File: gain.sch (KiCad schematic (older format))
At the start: 9 parts, among them U11 NE5532

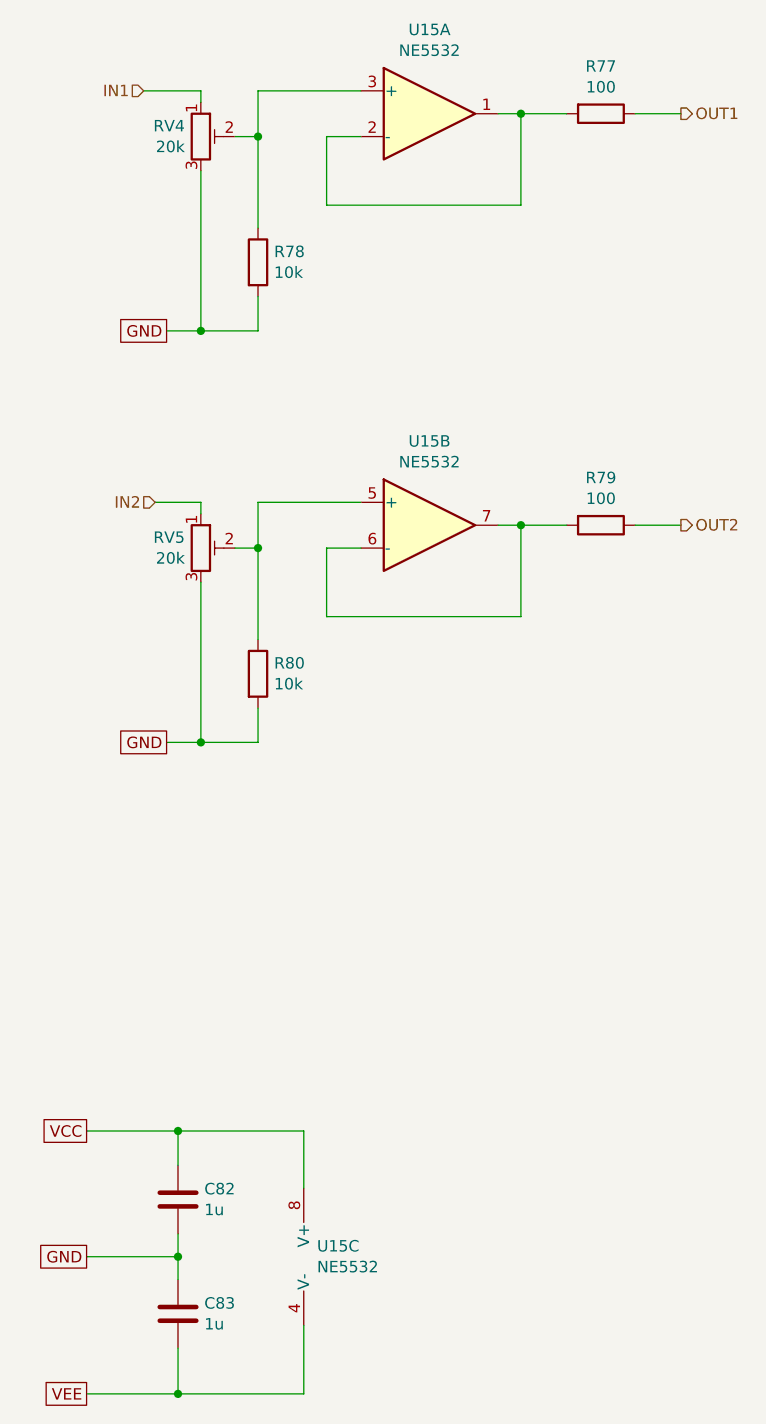
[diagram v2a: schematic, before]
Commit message: inverted LF processing chain, now with BW2 subsonic filter
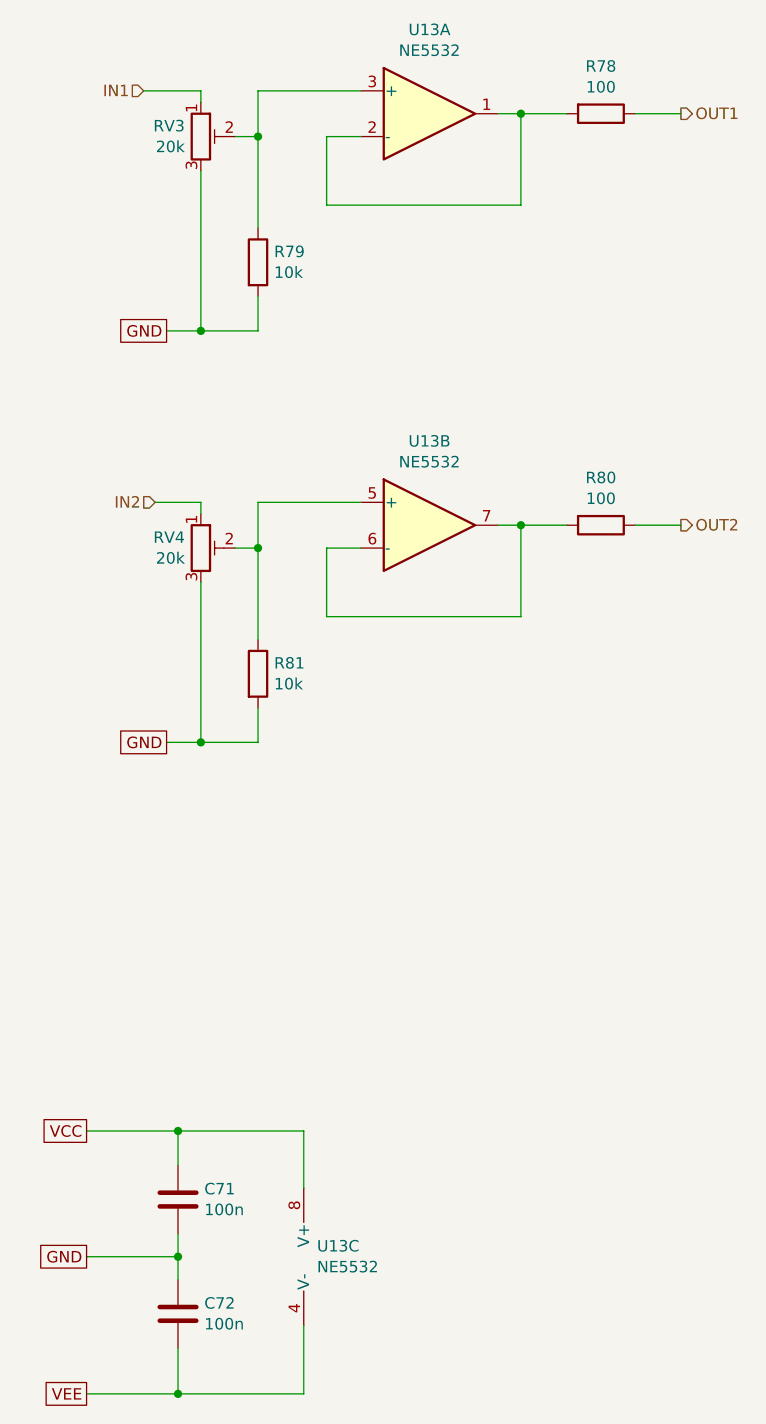
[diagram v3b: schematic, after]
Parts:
- C59: renamed from C58; value 1u -> 100n
- C60: renamed from C59; value 1u -> 100n
- renumbered RV2 to RV1, RV3 to RV2
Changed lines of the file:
@@
 $Descr A4 11693 8268
 encoding utf-8
-Sheet 13 19
+Sheet 10 17
 Title "Output Gain Controls"
 Date "2021-10-03"
@@
 AR Path="/615C4B54/61606DFA" Ref="U?"  Part="3"
 AR Path="/61604458/61606DFA" Ref="U11"  Part="3"
-AR Path="/6164D7C0/61606DFA" Ref="U15"  Part="3"
+AR Path="/6164D7C0/61606DFA" Ref="U13"  Part="3"
 AR Path="/61651AA2/61606DFA" Ref="U?"  Part="3"
-F 0 "U15" H 2808 6846 50  0000 L CNN
+F 0 "U13" H 2808 6846 50  0000 L CNN
 F 1 "NE5532" H 2808 6755 50  0000 L CNN
 F 2 "Housings_DIP:DIP-8_W7.62mm_Socket" H 2850 6800 50  0001 C CNN
@@
 AR Path="/61597701/61606E00" Ref="C?"  Part="1"
 AR Path="/615C4B54/61606E00" Ref="C?"  Part="1"
-AR Path="/61604458/61606E00" Ref="C59"  Part="1"
-AR Path="/6164D7C0/61606E00" Ref="C83"  Part="1"
+AR Path="/61604458/61606E00" Ref="C60"  Part="1"
+AR Path="/6164D7C0/61606E00" Ref="C72"  Part="1"
 AR Path="/61651AA2/61606E00" Ref="C?"  Part="1"
-F 0 "C83" H 2315 7096 50  0000 L CNN
-F 1 "1u" H 2315 7005 50  0000 L CNN
+F 0 "C72" H 2315 7096 50  0000 L CNN
+F 1 "100n" H 2315 7005 50  0000 L CNN
 F 2 "Capacitors_SMD:C_0805" H 2238 6900 50  0001 C CNN
 F 3 "~" H 2200 7050 50  0001 C CNN
@@
 AR Path="/61597701/61606E06" Ref="C?"  Part="1"
 AR Path="/615C4B54/61606E06" Ref="C?"  Part="1"
-AR Path="/61604458/61606E06" Ref="C58"  Part="1"
-AR Path="/6164D7C0/61606E06" Ref="C82"  Part="1"
+AR Path="/61604458/61606E06" Ref="C59"  Part="1"
+AR Path="/6164D7C0/61606E06" Ref="C71"  Part="1"
 AR Path="/61651AA2/61606E06" Ref="C?"  Part="1"
-F 0 "C82" H 2315 6596 50  0000 L CNN
-F 1 "1u" H 2315 6505 50  0000 L CNN
+F 0 "C71" H 2315 6596 50  0000 L CNN
+F 1 "100n" H 2315 6505 50  0000 L CNN
 F 2 "Capacitors_SMD:C_0805" H 2238 6400 50  0001 C CNN
 F 3 "~" H 2200 6550 50  0001 C CNN
@@
 P 3300 1800
 AR Path="/61604458/6160713F" Ref="U11"  Part="1"
-AR Path="/6164D7C0/6160713F" Ref="U15"  Part="1"
+AR Path="/6164D7C0/6160713F" Ref="U13"  Part="1"
 AR Path="/61651AA2/6160713F" Ref="U?"  Part="1"
-F 0 "U15" H 3300 2167 50  0000 C CNN
+F 0 "U13" H 3300 2167 50  0000 C CNN
 F 1 "NE5532" H 3300 2076 50  0000 C CNN
 F 2 "" H 3300 1800 50  0001 C CNN
@@
 P 3300 3600
 AR Path="/61604458/61607B4F" Ref="U11"  Part="2"
-AR Path="/6164D7C0/61607B4F" Ref="U15"  Part="2"
+AR Path="/6164D7C0/61607B4F" Ref="U13"  Part="2"
 AR Path="/61651AA2/61607B4F" Ref="U?"  Part="2"
-F 0 "U15" H 3300 3967 50  0000 C CNN
+F 0 "U13" H 3300 3967 50  0000 C CNN
 F 1 "NE5532" H 3300 3876 50  0000 C CNN
 F 2 "" H 3300 3600 50  0001 C CNN
@@
 $EndComp
 $Comp
-L Device:R_POT_TRIM RV2
+L Device:R_POT_TRIM RV1
 U 1 1 6160B080
 P 2300 1900
-AR Path="/61604458/6160B080" Ref="RV2"  Part="1"
-AR Path="/6164D7C0/6160B080" Ref="RV4"  Part="1"
+AR Path="/61604458/6160B080" Ref="RV1"  Part="1"
+AR Path="/6164D7C0/6160B080" Ref="RV3"  Part="1"
 AR Path="/61651AA2/6160B080" Ref="RV?"  Part="1"
-F 0 "RV4" H 2230 1946 50  0000 R CNN
+F 0 "RV3" H 2230 1946 50  0000 R CNN
 F 1 "20k" H 2230 1855 50  0000 R CNN
 F 2 "Potentiometers:Potentiometer_Trimmer_Bourns_3296W" H 2300 1900 50  0001 C CNN
@@
 P 2550 2450
 AR Path="/61604458/6160B89B" Ref="R54"  Part="1"
-AR Path="/6164D7C0/6160B89B" Ref="R78"  Part="1"
+AR Path="/6164D7C0/6160B89B" Ref="R79"  Part="1"
 AR Path="/61651AA2/6160B89B" Ref="R?"  Part="1"
-F 0 "R78" H 2620 2496 50  0000 L CNN
+F 0 "R79" H 2620 2496 50  0000 L CNN
 F 1 "10k" H 2620 2405 50  0000 L CNN
 F 2 "Resistors_SMD:R_0805" V 2480 2450 50  0001 C CNN
@@
 	2300 1700 2300 1750
 $Comp
-L Device:R_POT_TRIM RV3
+L Device:R_POT_TRIM RV2
 U 1 1 61627D7A
 P 2300 3700
-AR Path="/61604458/61627D7A" Ref="RV3"  Part="1"
-AR Path="/6164D7C0/61627D7A" Ref="RV5"  Part="1"
+AR Path="/61604458/61627D7A" Ref="RV2"  Part="1"
+AR Path="/6164D7C0/61627D7A" Ref="RV4"  Part="1"
 AR Path="/61651AA2/61627D7A" Ref="RV?"  Part="1"
-F 0 "RV5" H 2230 3746 50  0000 R CNN
+F 0 "RV4" H 2230 3746 50  0000 R CNN
 F 1 "20k" H 2230 3655 50  0000 R CNN
 F 2 "Potentiometers:Potentiometer_Trimmer_Bourns_3296W" H 2300 3700 50  0001 C CNN
@@
 P 2550 4250
 AR Path="/61604458/61627D80" Ref="R56"  Part="1"
-AR Path="/6164D7C0/61627D80" Ref="R80"  Part="1"
+AR Path="/6164D7C0/61627D80" Ref="R81"  Part="1"
 AR Path="/61651AA2/61627D80" Ref="R?"  Part="1"
-F 0 "R80" H 2620 4296 50  0000 L CNN
+F 0 "R81" H 2620 4296 50  0000 L CNN
 F 1 "10k" H 2620 4205 50  0000 L CNN
 F 2 "Resistors_SMD:R_0805" V 2480 4250 50  0001 C CNN
@@
 P 4050 1800
 AR Path="/61604458/61636763" Ref="R53"  Part="1"
-AR Path="/6164D7C0/61636763" Ref="R77"  Part="1"
+AR Path="/6164D7C0/61636763" Ref="R78"  Part="1"
 AR Path="/61651AA2/61636763" Ref="R?"  Part="1"
-F 0 "R77" V 3843 1800 50  0000 C CNN
+F 0 "R78" V 3843 1800 50  0000 C CNN
 F 1 "100" V 3934 1800 50  0000 C CNN
 F 2 "Resistors_SMD:R_0805" V 3980 1800 50  0001 C CNN
@@
 P 4050 3600
 AR Path="/61604458/6163D415" Ref="R55"  Part="1"
-AR Path="/6164D7C0/6163D415" Ref="R79"  Part="1"
+AR Path="/6164D7C0/6163D415" Ref="R80"  Part="1"
 AR Path="/61651AA2/6163D415" Ref="R?"  Part="1"
-F 0 "R79" V 3843 3600 50  0000 C CNN
+F 0 "R80" V 3843 3600 50  0000 C CNN
 F 1 "100" V 3934 3600 50  0000 C CNN
 F 2 "Resistors_SMD:R_0805" V 3980 3600 50  0001 C CNN
